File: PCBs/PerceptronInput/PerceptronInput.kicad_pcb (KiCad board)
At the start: 2 copper layers, 164 x 86 mm, 54 parts, among them J1 Conn_02x10, J2 Conn_01x04_Pin, SW1 SW_DPDT, SW10 SW_DPDT, SW11 SW_DPDT, SW12 SW_DPDT, SW13 SW_DPDT, SW14 SW_DPDT, SW15 SW_DPDT, SW16 SW_DPDT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

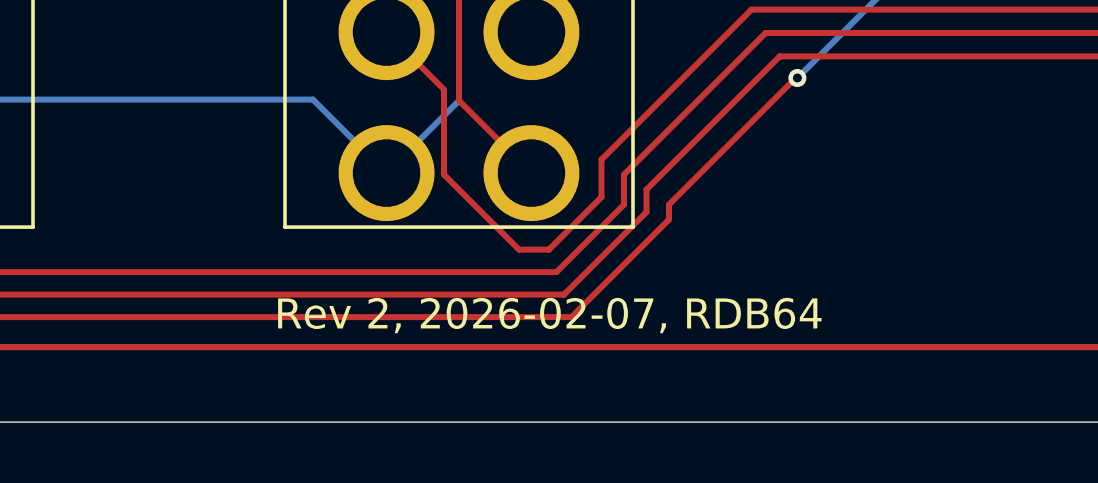
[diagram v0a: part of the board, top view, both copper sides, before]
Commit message: Get rid of jlc silkscreen.
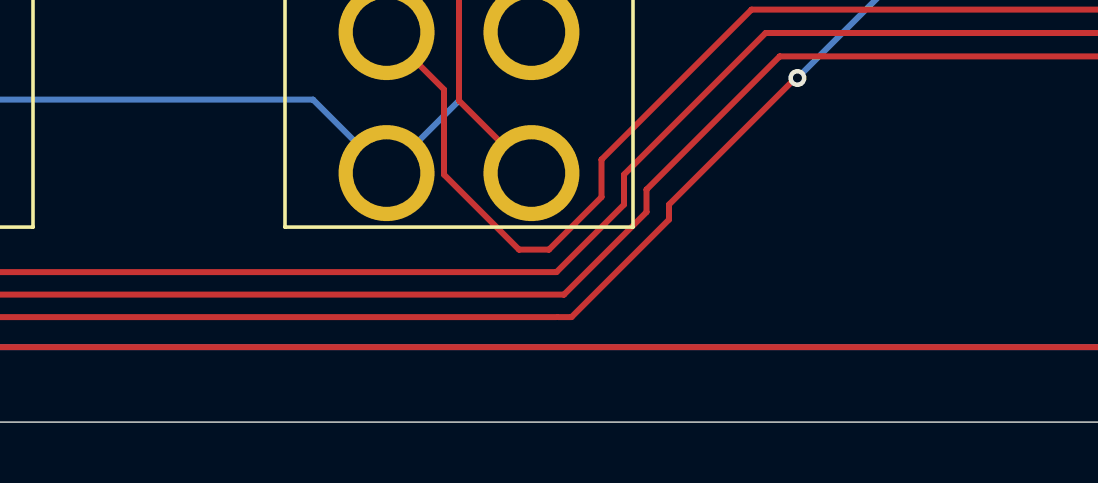
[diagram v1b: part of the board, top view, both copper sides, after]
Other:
- board text removed: "jlcjlcjlcjlc"
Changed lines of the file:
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@@
 	(title_block
 		(title "Perceptron Input")
-		(date "2026-02-07")
-		(rev "2")
+		(date "2026-02-20")
+		(rev "2.1")
 		(company "RDB64")
 	)
@@
 		)
 	)
-	(gr_text "Rev ${REVISION}, ${ISSUE_DATE}, ${COMPANY}"
-		(at 143 150 0)
-		(layer "F.SilkS")
-		(effects
-			(font
-				(size 1 1)
-				(thickness 0.1)
-			)
-			(justify bottom)
-		)
-	)
 	(gr_text "Negative Indicator LED"
 		(at 177.5 147.5 0)
@@
 		)
 	)
+	(gr_text "Rev ${REVISION}, ${ISSUE_DATE}, ${COMPANY}"
+		(at 62.75 129.75 270)
+		(layer "B.SilkS")
+		(effects
+			(font
+				(size 1 1)
+				(thickness 0.1)
+			)
+			(justify bottom mirror)
+		)
+	)
 	(gr_text "To Adder"
 		(at 213.46 110 90)
@@
 		)
 	)
-	(gr_text "jlcjlcjlcjlc"
-		(at 75 150 0)
-		(layer "B.SilkS")
-		(effects
-			(font
-				(size 1 1)
-				(thickness 0.1)
-			)
-			(justify right bottom mirror)
-		)
-	)
